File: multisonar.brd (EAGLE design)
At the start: 160 x 100 mm, 0 parts

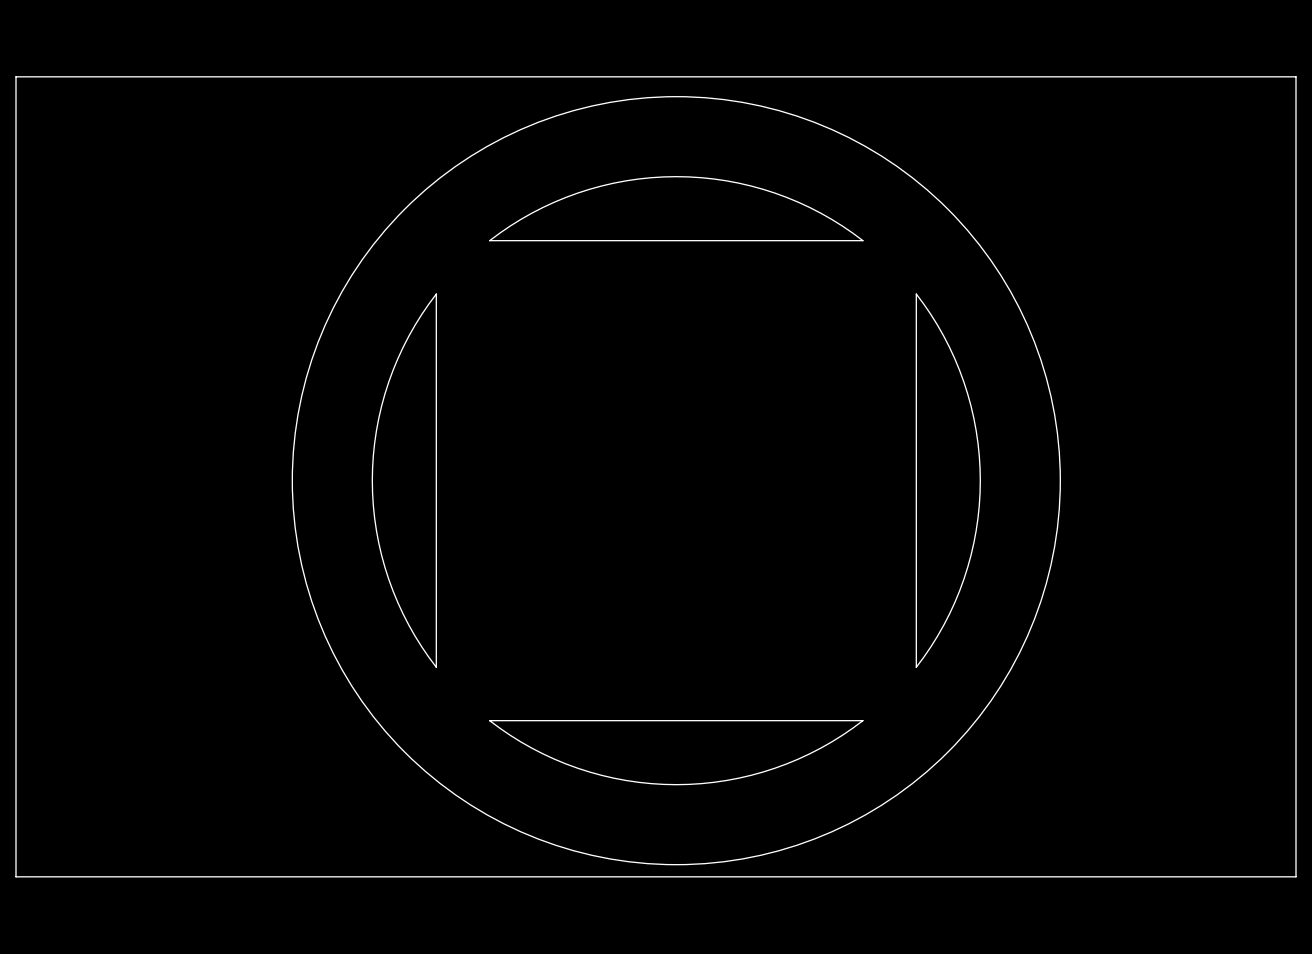
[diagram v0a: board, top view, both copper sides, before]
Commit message: Add ultrasonic sensors
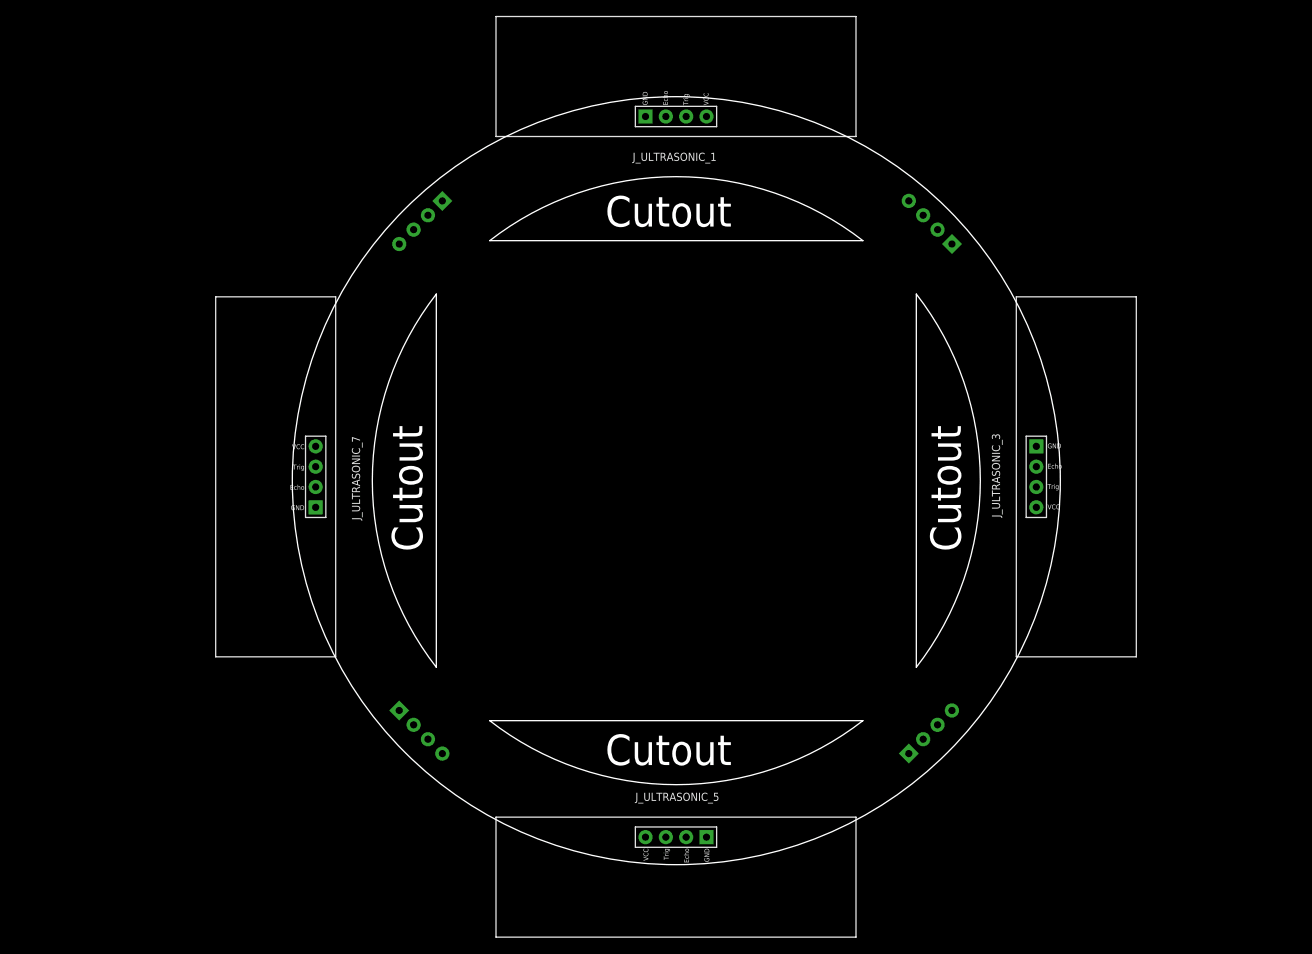
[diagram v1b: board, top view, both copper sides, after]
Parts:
- added J_ULTRASONIC_1, J_ULTRASONIC_2, J_ULTRASONIC_3, J_ULTRASONIC_4, J_ULTRASONIC_5, J_ULTRASONIC_6, J_ULTRASONIC_7, J_ULTRASONIC_8: HC-SR04, Ultrasonic Sensor HC-SR04:HC-SR04_FOOTPRINT
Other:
- board size 160 x 100 mm -> 96 x 96 mm
- board text added: "Cutout"
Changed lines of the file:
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@@
 <setting verticaltext="up"/>
 </settings>
-<grid distance="50" unitdist="mil" unit="mm" style="lines" multiple="1" display="no" altdistance="5" altunitdist="mil" altunit="mil"/>
+<grid distance="2.5" unitdist="mm" unit="mm" style="lines" multiple="1" display="yes" altdistance="5" altunitdist="mil" altunit="mil"/>
 <layers>
 <layer number="1" name="Top" color="4" fill="1" visible="yes" active="yes"/>
@@
 <board>
 <plain>
-<wire x1="0" y1="0" x2="160" y2="0" width="0" layer="20"/>
-<wire x1="160" y1="0" x2="160" y2="100" width="0" layer="20"/>
-<wire x1="160" y1="100" x2="0" y2="100" width="0" layer="20"/>
-<wire x1="0" y1="100" x2="0" y2="0" width="0" layer="20"/>
 <wire x1="52.54" y1="72.843809375" x2="52.54" y2="26.196190625" width="0.001" layer="20"/>
 <circle x="82.54" y="49.52" radius="48" width="0.001" layer="20"/>
@@
 <wire x1="52.54" y1="72.843809375" x2="52.54" y2="26.196190625" width="0.001" layer="20" curve="75.727297"/>
 <wire x1="105.863809375" y1="79.52" x2="59.216190625" y2="79.52" width="0.001" layer="20" curve="75.727297"/>
+<text x="73.66" y="13.97" size="3.81" layer="20" font="vector">Cutout</text>
+<text x="73.66" y="81.28" size="3.81" layer="20" font="vector">Cutout</text>
+<text x="118.11" y="40.64" size="3.81" layer="20" font="vector" rot="R90">Cutout</text>
+<text x="50.8" y="40.64" size="3.81" layer="20" font="vector" rot="R90">Cutout</text>
 </plain>
 <attributes>
@@
 </class>
 </classes>
-<designrules name="default">
+<designrules name="SeeedStudio_2layer_DRU_edited">
 <description language="de">&lt;b&gt;EAGLE Design Rules&lt;/b&gt;
 &lt;p&gt;
@@
 necessary adjustments and save your customized
 design rules under a new name.</description>
+<description language="zh">&lt;b&gt;Seeed Studio EAGLE Design Rules&lt;/b&gt;
+</description>
 <param name="layerSetup" value="(1*16)"/>
-<param name="mtCopper" value="0.035mm 0.035mm 0.035mm 0.035mm 0.035mm 0.035mm 0.035mm 0.035mm 0.035mm 0.035mm 0.035mm 0.035mm 0.035mm 0.035mm 0.035mm 0.035mm"/>
-<param name="mtIsolate" value="1.5mm 0.15mm 0.2mm 0.15mm 0.2mm 0.15mm 0.2mm 0.15mm 0.2mm 0.15mm 0.2mm 0.15mm 0.2mm 0.15mm 0.2mm"/>
+<param name="mtCopper" value="0.035mm 0.0175mm 0.035mm 0.035mm 0.035mm 0.035mm 0.035mm 0.035mm 0.035mm 0.035mm 0.035mm 0.035mm 0.035mm 0.035mm 0.0175mm 0.035mm"/>
+<param name="mtIsolate" value="1.5mm 1.1mm 0.2mm 0.15mm 0.2mm 0.15mm 0.2mm 0.15mm 0.2mm 0.15mm 0.2mm 0.15mm 0.2mm 0.15mm 0.2mm"/>
 <param name="mdWireWire" value="6mil"/>
 <param name="mdWirePad" value="6mil"/>
@@
 <param name="mdPadVia" value="6mil"/>
 <param name="mdViaVia" value="6mil"/>
-<param name="mdSmdPad" value="6mil"/>
-<param name="mdSmdVia" value="6mil"/>
-<param name="mdSmdSmd" value="6mil"/>
-<param name="mdViaViaSameLayer" value="6mil"/>
+<param name="mdSmdPad" value="0mil"/>
+<param name="mdSmdVia" value="0mil"/>
+<param name="mdSmdSmd" value="0mil"/>
+<param name="mdViaViaSameLayer" value="8mil"/>
 <param name="mnLayersViaInSmd" value="2"/>
-<param name="mdCopperDimension" value="40mil"/>
-<param name="mdDrill" value="6mil"/>
+<param name="mdCopperDimension" value="10mil"/>
+<param name="mdDrill" value="10mil"/>
 <param name="mdSmdStop" value="0mil"/>
-<param name="msWidth" value="6mil"/>
-<param name="msDrill" value="0.35mm"/>
-<param name="msMicroVia" value="9.99mm"/>
-<param name="msBlindViaRatio" value="0.5"/>
+<param name="msWidth" value="7mil"/>
+<param name="msDrill" value="15mil"/>
+<param name="msMicroVia" value="15mil"/>
+<param name="msBlindViaRatio" value="1"/>
 <param name="rvPadTop" value="0.25"/>
 <param name="rvPadInner" value="0.25"/>
@@
 <param name="rlMinPadBottom" value="10mil"/>
 <param name="rlMaxPadBottom" value="20mil"/>
-<param name="rlMinViaOuter" value="8mil"/>
+<param name="rlMinViaOuter" value="6mil"/>
 <param name="rlMaxViaOuter" value="20mil"/>
-<param name="rlMinViaInner" value="8mil"/>
+<param name="rlMinViaInner" value="6mil"/>
 <param name="rlMaxViaInner" value="20mil"/>
 <param name="rlMinMicroViaOuter" value="4mil"/>
@@
 <param name="psTop" value="-1"/>
 <param name="psBottom" value="-1"/>
-<param name="psFirst" value="-1"/>
+<param name="psFirst" value="0"/>
 <param name="psElongationLong" value="100"/>
 <param name="psElongationOffset" value="100"/>
 <param name="mvStopFrame" value="1"/>
 <param name="mvCreamFrame" value="0"/>
-<param name="mlMinStopFrame" value="4mil"/>
-<param name="mlMaxStopFrame" value="4mil"/>
+<param name="mlMinStopFrame" value="2mil"/>
+<param name="mlMaxStopFrame" value="2mil"/>
 <param name="mlMinCreamFrame" value="0mil"/>
 <param name="mlMaxCreamFrame" value="0mil"/>
-<param name="mlViaStopLimit" value="0mil"/>
+<param name="mlViaStopLimit" value="100mil"/>
 <param name="srRoundness" value="0"/>
 <param name="srMinRoundness" value="0mil"/>
@@
 <param name="checkAngle" value="0"/>
 <param name="checkFont" value="1"/>
-<param name="checkRestrict" value="1"/>
+<param name="checkRestrict" value="0"/>
 <param name="useDiameter" value="13"/>
 <param name="maxErrors" value="50"/>
@@
 </autorouter>
 <elements>
+<element name="J_ULTRASONIC_1" library="Ultrasonic Sensor HC-SR04" package="HC-SR04_FOOTPRINT" value="HC-SR04" x="82.5" y="92.5" rot="R90"/>
+<element name="J_ULTRASONIC_2" library="Ultrasonic Sensor HC-SR04" package="HC-SR04_FOOTPRINT" value="HC-SR04" x="112.5" y="80" rot="MR135"/>
+<element name="J_ULTRASONIC_3" library="Ultrasonic Sensor HC-SR04" package="HC-SR04_FOOTPRINT" value="HC-SR04" x="125" y="50"/>
+<element name="J_ULTRASONIC_8" library="Ultrasonic Sensor HC-SR04" package="HC-SR04_FOOTPRINT" value="HC-SR04" x="52.395925" y="80" rot="MR45"/>
+<element name="J_ULTRASONIC_5" library="Ultrasonic Sensor HC-SR04" package="HC-SR04_FOOTPRINT" value="HC-SR04" x="82.5" y="7.5" rot="R270"/>
+<element name="J_ULTRASONIC_6" library="Ultrasonic Sensor HC-SR04" package="HC-SR04_FOOTPRINT" value="HC-SR04" x="52.395925" y="19.895921875" rot="MR315"/>
+<element name="J_ULTRASONIC_7" library="Ultrasonic Sensor HC-SR04" package="HC-SR04_FOOTPRINT" value="HC-SR04" x="40" y="50" rot="R180"/>
+<element name="J_ULTRASONIC_4" library="Ultrasonic Sensor HC-SR04" package="HC-SR04_FOOTPRINT" value="HC-SR04" x="112.5" y="19.895921875" rot="MR225"/>
 </elements>
 <signals>
